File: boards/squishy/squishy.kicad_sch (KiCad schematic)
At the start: 69 parts, among them J10 QXH-060, J2 Conn_02x20_Odd_Even_Shielded, J3 MEM2061-01-188-00-A, J8 TRIGGER, J9 REFCLK, SW2 DFU, U1 LFE5UM5G-45F-8BG381C, U2 GD25Q64EWIGR, U6 ATSAMD09D14A-M, X1 48MHz

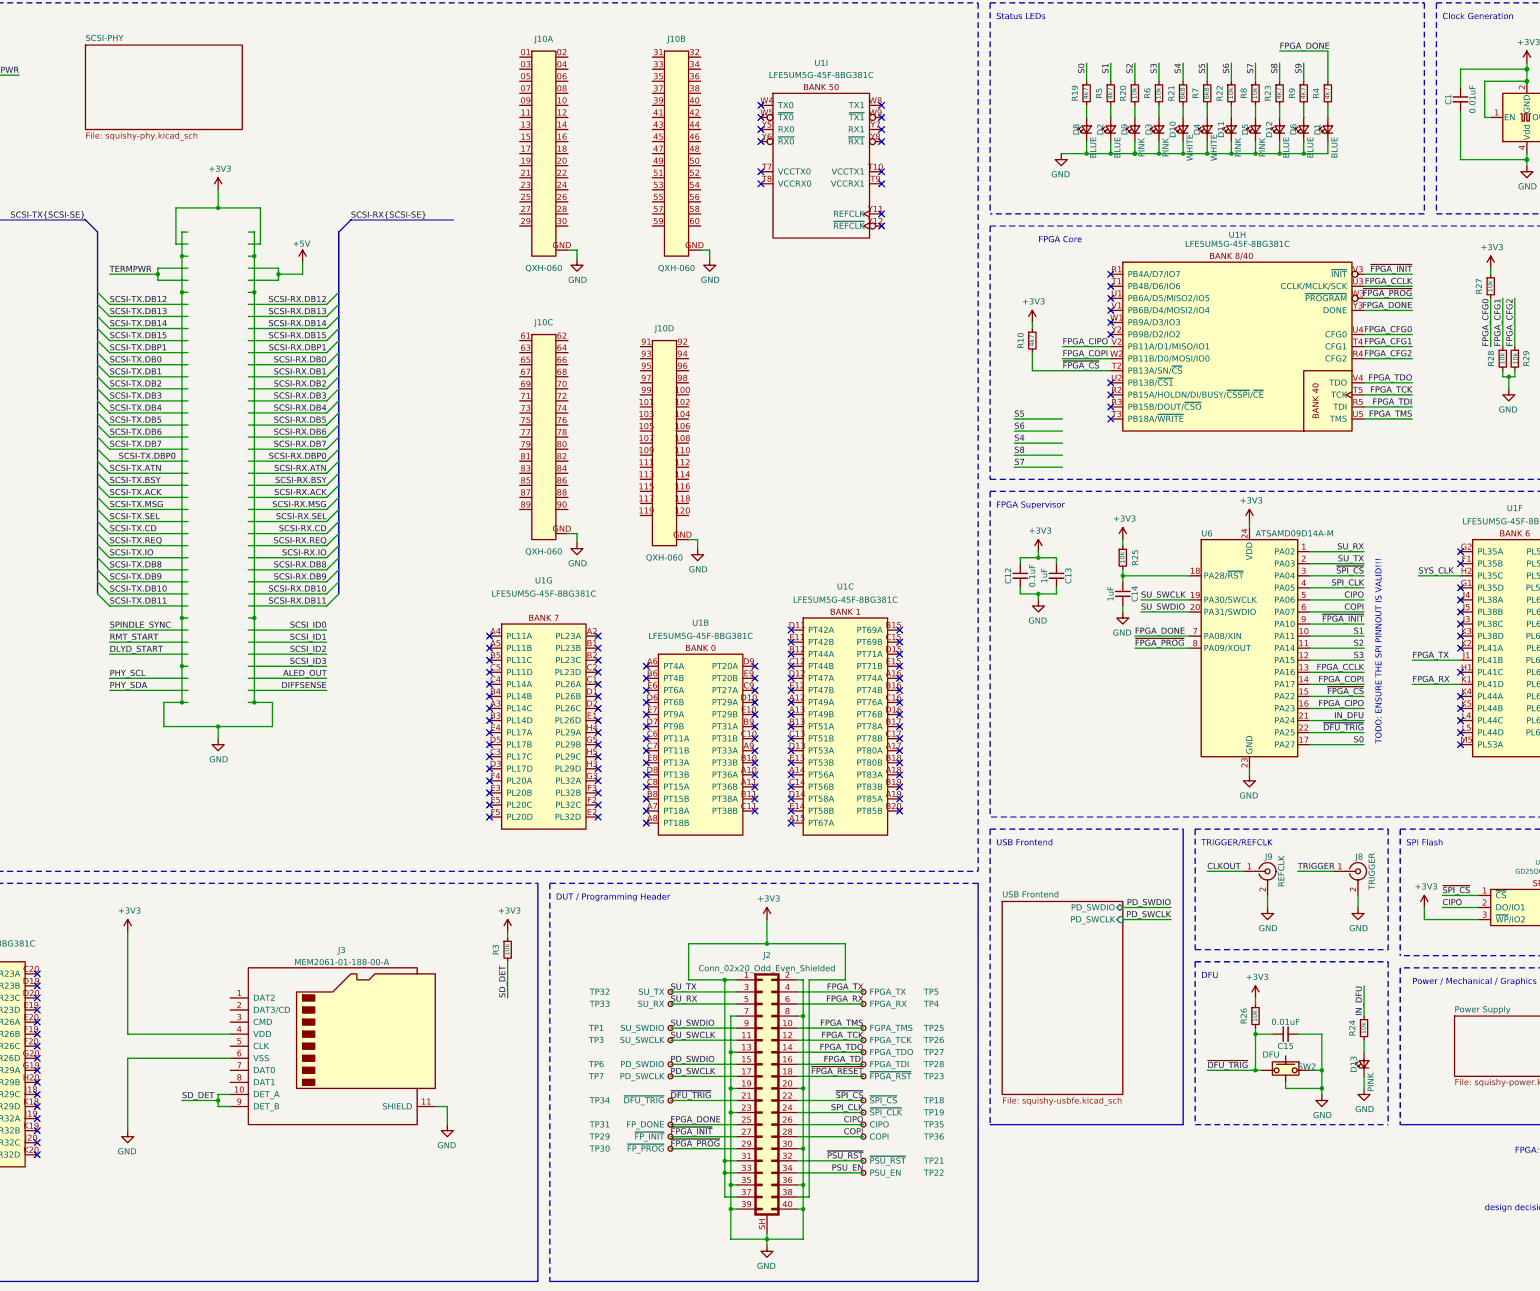
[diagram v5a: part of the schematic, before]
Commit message: hardware: fixed the USB PD controller pinout, as well as the AT SAMD symbol
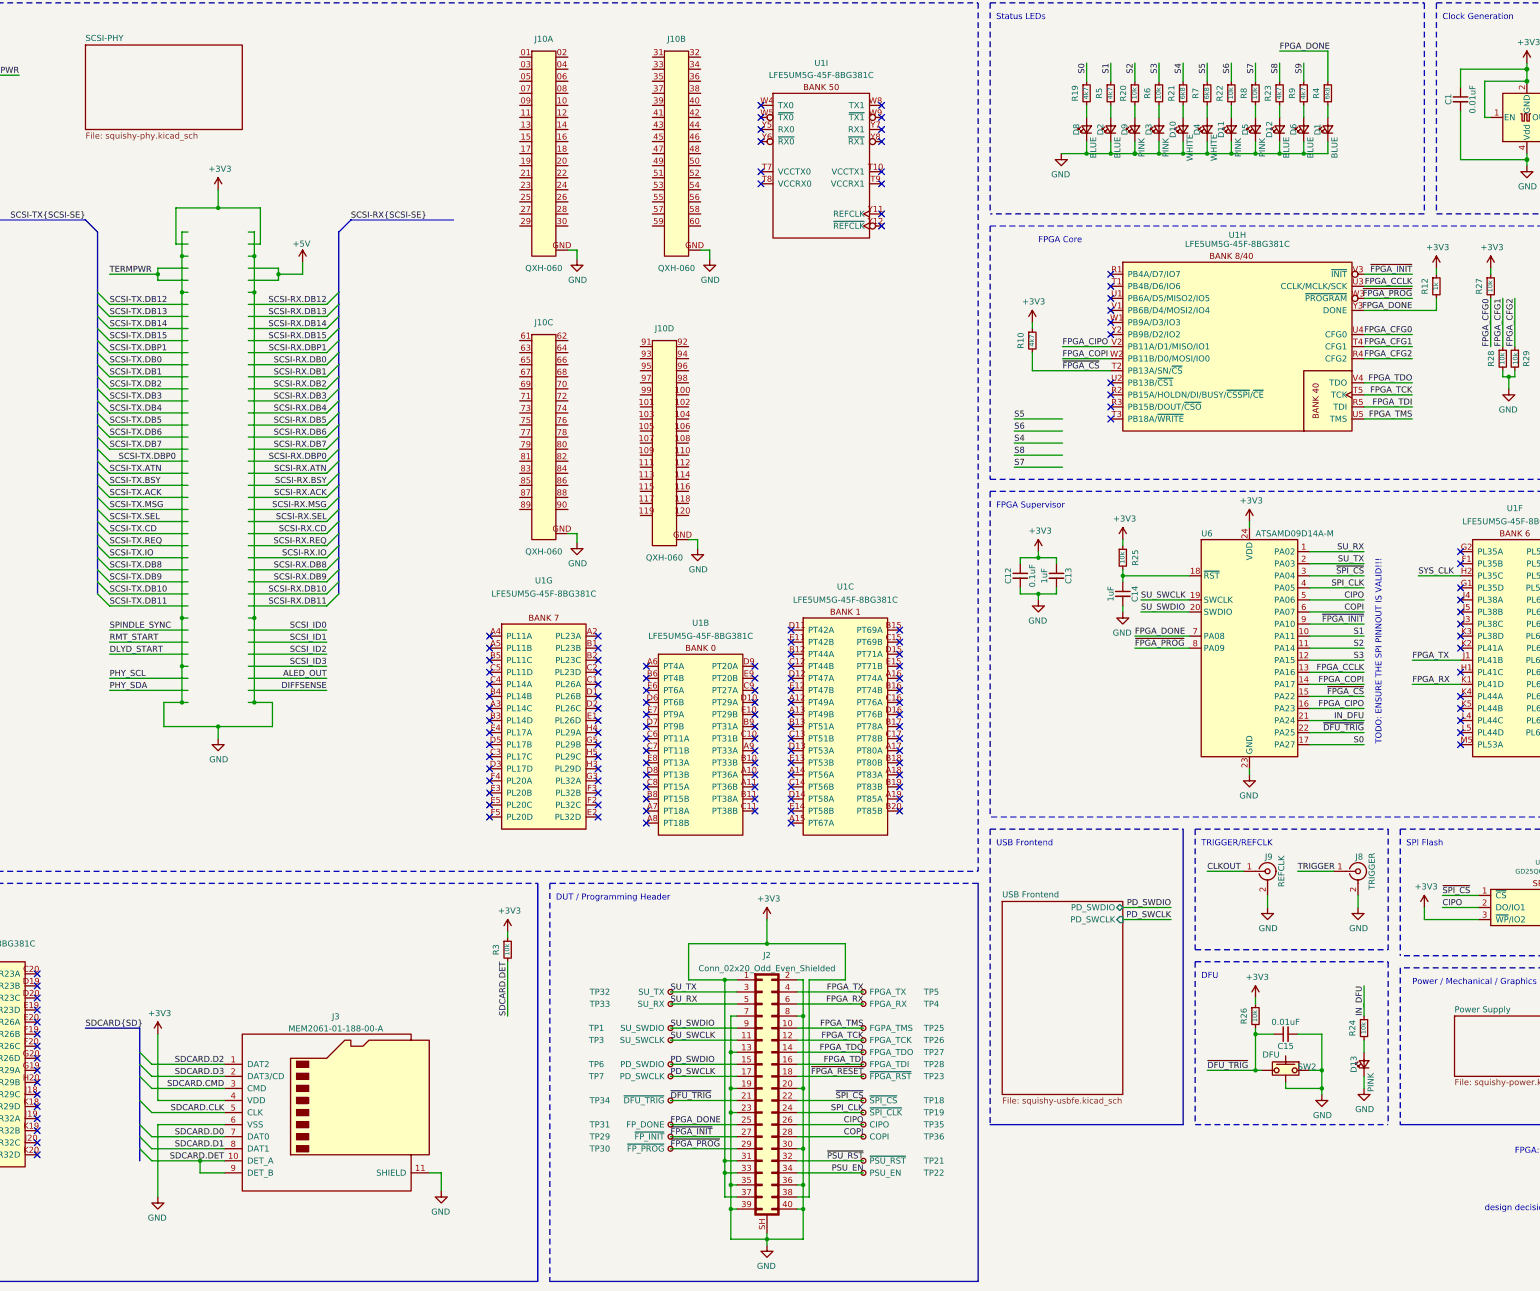
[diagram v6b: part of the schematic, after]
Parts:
- added R12: 1k, Resistor_SMD:R_0603_1608Metric, symbol Device:R_Small
- R4: value 4k7 -> 6k8; MFR Vishay Dale -> (none); MPN CRCW06034K70FKEA -> (none)
- U6: symbol MCU_Microchip_SAMD:ATSAMD09D14A-M -> lethalbit:ATSAMD09D14A-M
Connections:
- net +3V3: now also R12.1
- net FPGA_DONE: now also R12.2
- net GND: now also U6.25 (GND)
- net SDCARD.D2: now reaches J3.1 (DAT2)
- net SDCARD.D3: now reaches J3.2 (DAT3/CD)
- net SDCARD.CMD: now reaches J3.3 (CMD)
- net SDCARD.CLK: now reaches J3.5 (CLK)
- net SDCARD.D0: now reaches J3.7 (DAT0)
- net SDCARD.D1: now reaches J3.8 (DAT1)
- net SD_DET renamed SDCARD.DET
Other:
- moved on the sheet: J3

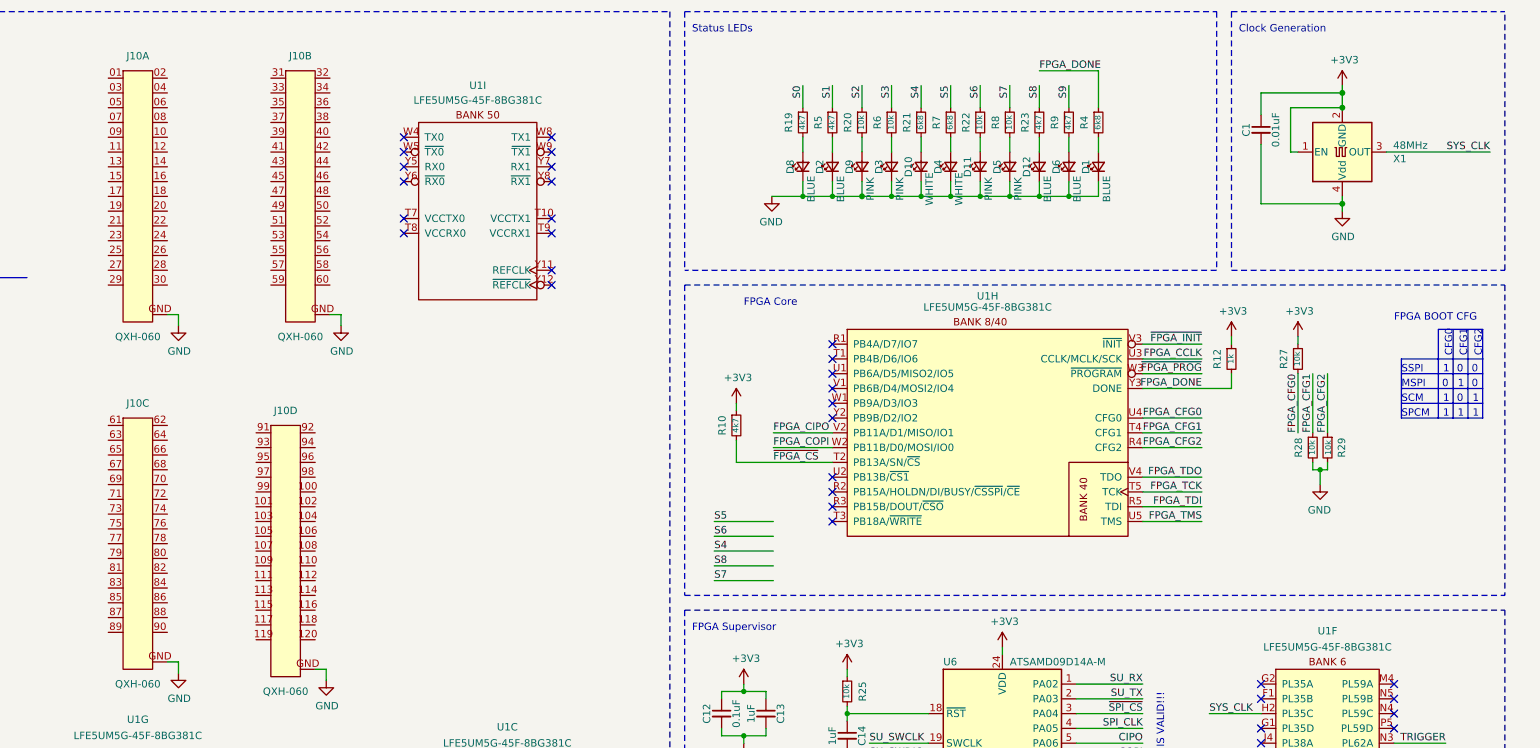
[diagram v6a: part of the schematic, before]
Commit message: hardware: squishy: some minor ERC fixes
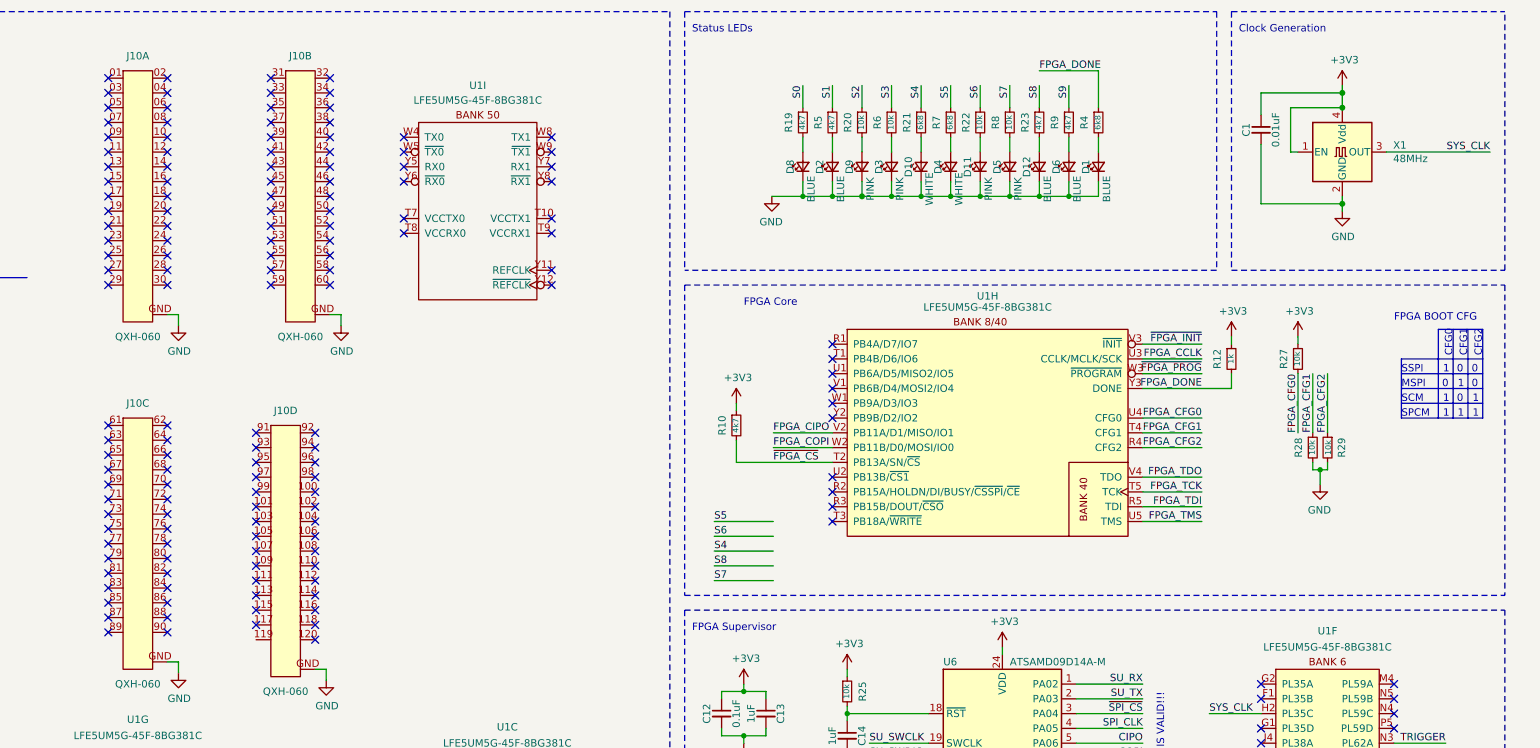
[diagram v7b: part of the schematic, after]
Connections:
- net +3V3: now also X1.4 (Vdd); no longer X1.2 (GND)
- net GND: now also X1.2 (GND); no longer X1.4 (Vdd)
- no-connect marks 176 -> 295
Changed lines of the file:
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@@
   (no_connect (at 193.04 156.21))
   (no_connect (at 193.04 186.69))
+  (no_connect (at 166.37 43.18))
+  (no_connect (at 166.37 48.26))
+  (no_connect (at 166.37 45.72))
+  (no_connect (at 201.93 86.36))
+  (no_connect (at 204.47 38.1))
+  (no_connect (at 204.47 40.64))
+  (no_connect (at 204.47 43.18))
+  (no_connect (at 204.47 45.72))
+  (no_connect (at 204.47 25.4))
+  (no_connect (at 204.47 27.94))
+  (no_connect (at 204.47 30.48))
+  (no_connect (at 204.47 33.02))
+  (no_connect (at 204.47 35.56))
+  (no_connect (at 194.31 35.56))
+  (no_connect (at 194.31 45.72))
+  (no_connect (at 194.31 43.18))
+  (no_connect (at 194.31 40.64))
+  (no_connect (at 194.31 38.1))
+  (no_connect (at 194.31 25.4))
+  (no_connect (at 194.31 27.94))
+  (no_connect (at 194.31 30.48))
+  (no_connect (at 194.31 33.02))
+  (no_connect (at 201.93 96.52))
+  (no_connect (at 201.93 88.9))
+  (no_connect (at 201.93 91.44))
+  (no_connect (at 201.93 93.98))
+  (no_connect (at 194.31 58.42))
+  (no_connect (at 194.31 55.88))
+  (no_connect (at 194.31 53.34))
+  (no_connect (at 194.31 50.8))
+  (no_connect (at 194.31 48.26))
+  (no_connect (at 204.47 48.26))
+  (no_connect (at 204.47 53.34))
+  (no_connect (at 204.47 50.8))
+  (no_connect (at 204.47 58.42))
+  (no_connect (at 204.47 55.88))
+  (no_connect (at 194.31 60.96))
+  (no_connect (at 204.47 60.96))
+  (no_connect (at 201.93 109.22))
+  (no_connect (at 191.77 106.68))
+  (no_connect (at 191.77 109.22))
+  (no_connect (at 201.93 99.06))
+  (no_connect (at 201.93 101.6))
+  (no_connect (at 201.93 104.14))
+  (no_connect (at 201.93 106.68))
+  (no_connect (at 201.93 111.76))
+  (no_connect (at 201.93 114.3))
+  (no_connect (at 201.93 119.38))
+  (no_connect (at 201.93 121.92))
+  (no_connect (at 201.93 116.84))
+  (no_connect (at 191.77 111.76))
+  (no_connect (at 191.77 114.3))
+  (no_connect (at 191.77 119.38))
+  (no_connect (at 191.77 116.84))
   (no_connect (at 290.83 76.2))
   (no_connect (at 290.83 93.98))
@@
   (no_connect (at 290.83 99.06))
   (no_connect (at 290.83 101.6))
+  (no_connect (at 176.53 87.63))
+  (no_connect (at 166.37 87.63))
+  (no_connect (at 166.37 85.09))
+  (no_connect (at 176.53 85.09))
+  (no_connect (at 176.53 90.17))
+  (no_connect (at 191.77 96.52))
+  (no_connect (at 191.77 99.06))
+  (no_connect (at 191.77 101.6))
+  (no_connect (at 191.77 104.14))
+  (no_connect (at 166.37 90.17))
+  (no_connect (at 166.37 92.71))
+  (no_connect (at 191.77 93.98))
+  (no_connect (at 191.77 91.44))
+  (no_connect (at 191.77 88.9))
+  (no_connect (at 191.77 86.36))
   (no_connect (at 387.35 142.24))
   (no_connect (at 387.35 144.78))
@@
   (no_connect (at 290.83 73.66))
   (no_connect (at 290.83 71.12))
+  (no_connect (at 166.37 118.11))
+  (no_connect (at 166.37 120.65))
+  (no_connect (at 176.53 105.41))
+  (no_connect (at 176.53 107.95))
+  (no_connect (at 176.53 92.71))
+  (no_connect (at 176.53 102.87))
+  (no_connect (at 166.37 97.79))
+  (no_connect (at 166.37 95.25))
+  (no_connect (at 176.53 100.33))
+  (no_connect (at 176.53 95.25))
+  (no_connect (at 176.53 97.79))
+  (no_connect (at 176.53 115.57))
+  (no_connect (at 176.53 110.49))
+  (no_connect (at 176.53 118.11))
+  (no_connect (at 176.53 113.03))
+  (no_connect (at 176.53 120.65))
+  (no_connect (at 166.37 100.33))
+  (no_connect (at 166.37 102.87))
+  (no_connect (at 166.37 105.41))
+  (no_connect (at 166.37 107.95))
+  (no_connect (at 166.37 113.03))
+  (no_connect (at 166.37 115.57))
+  (no_connect (at 166.37 110.49))
+  (no_connect (at 166.37 58.42))
+  (no_connect (at 166.37 60.96))
+  (no_connect (at 176.53 58.42))
+  (no_connect (at 176.53 60.96))
+  (no_connect (at 176.53 40.64))
+  (no_connect (at 176.53 38.1))
+  (no_connect (at 176.53 35.56))
+  (no_connect (at 176.53 33.02))
+  (no_connect (at 176.53 30.48))
+  (no_connect (at 176.53 27.94))
+  (no_connect (at 166.37 40.64))
+  (no_connect (at 166.37 50.8))
+  (no_connect (at 166.37 53.34))
+  (no_connect (at 166.37 55.88))
+  (no_connect (at 166.37 38.1))
+  (no_connect (at 166.37 35.56))
+  (no_connect (at 166.37 27.94))
+  (no_connect (at 166.37 30.48))
+  (no_connect (at 166.37 33.02))
+  (no_connect (at 176.53 55.88))
+  (no_connect (at 176.53 53.34))
+  (no_connect (at 176.53 43.18))
+  (no_connect (at 176.53 45.72))
+  (no_connect (at 176.53 48.26))
+  (no_connect (at 176.53 50.8))
+  (no_connect (at 176.53 25.4))
+  (no_connect (at 166.37 25.4))
   (no_connect (at 364.49 170.18))
   (no_connect (at 64.77 256.54))
@@
     (pin "1")
   )
-  (symbol (lib_id "Oscillator:ASE-xxxMHz") (at 378.46 38.1 0) (mirror x) (unit 1)
+  (symbol (lib_id "Oscillator:ASE-xxxMHz") (at 378.46 38.1 0) (unit 1)
     (in_bom yes) (on_board yes)
-    (property "Reference" "X1" (id 0) (at 387.1976 39.2684 0)
+    (property "Reference" "X1" (id 0) (at 387.1976 36.9316 0)
       (effects (font (size 1.27 1.27)) (justify left))
     )
-    (property "Value" "48MHz" (id 1) (at 387.1976 36.957 0)
+    (property "Value" "48MHz" (id 1) (at 387.1976 39.243 0)
       (effects (font (size 1.27 1.27)) (justify left))
     )
-    (property "Footprint" "rhais_osc:SMD3225" (id 2) (at 396.24 29.21 0)
+    (property "Footprint" "rhais_osc:SMD3225" (id 2) (at 396.24 46.99 0)
       (effects (font (size 1.27 1.27)) hide)
     )
